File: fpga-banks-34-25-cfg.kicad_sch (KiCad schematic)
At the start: 49 parts, among them J13 PinHeader_1x3_P2.54mm_Drill1.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, Q12 2N7002_SOT-23-3, Q13 2N7002_SOT-23-3, Q14 2N7002_SOT-23-3, Q15 2N7002_SOT-23-3, Q16 2N7002_SOT-23-3, U14 XC7A100T-FGG484

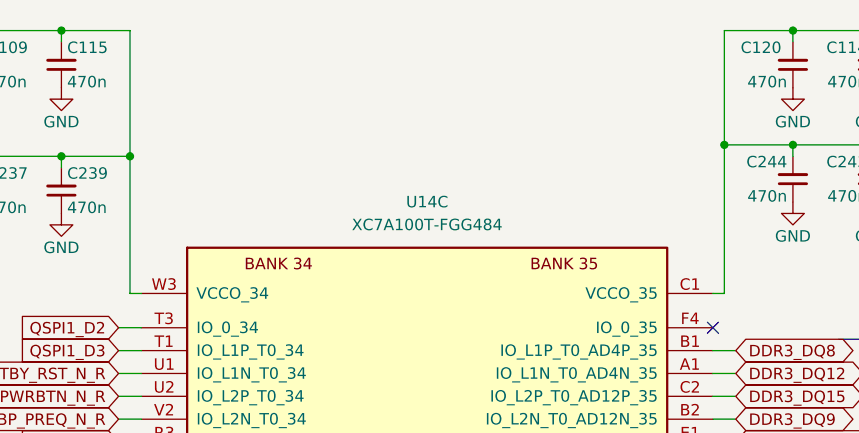
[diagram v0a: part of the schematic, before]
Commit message: ddr3 routing finished
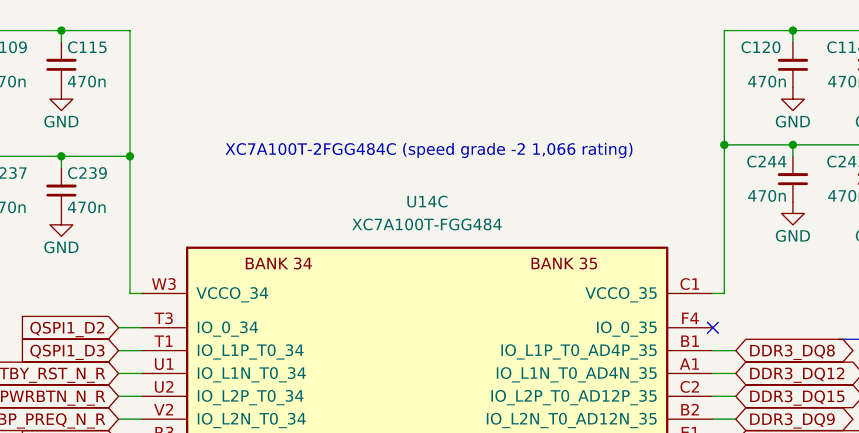
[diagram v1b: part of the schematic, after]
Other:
- note added: "XC7A100T-2FGG484C (speed grade -2 1,066 rating)"
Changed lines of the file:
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@@
+		)
+	)
+	(text "XC7A100T-2FGG484C (speed grade -2 1,066 rating)"
+		(exclude_from_sim no)
+		(at 299.974 57.912 0)
+		(effects
+			(font
+				(size 1.27 1.27)
+			)
 		)
 	)

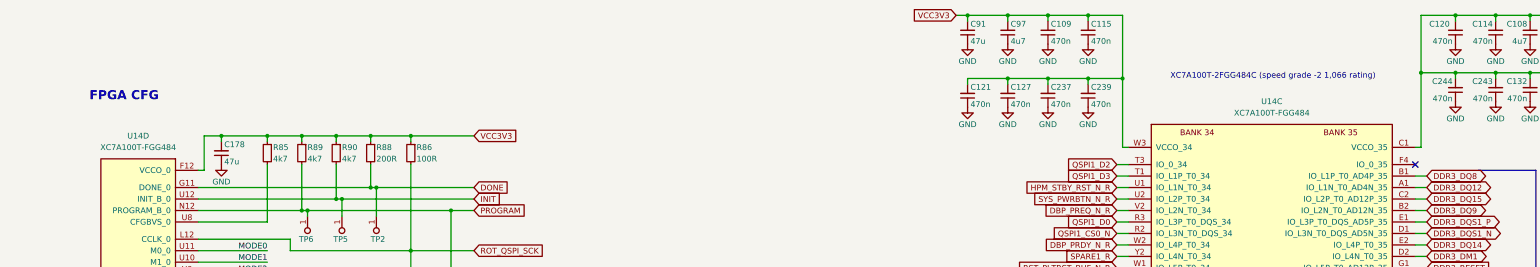
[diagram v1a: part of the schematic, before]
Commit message: a lot of routing and almost all caps of the fpga are placed down
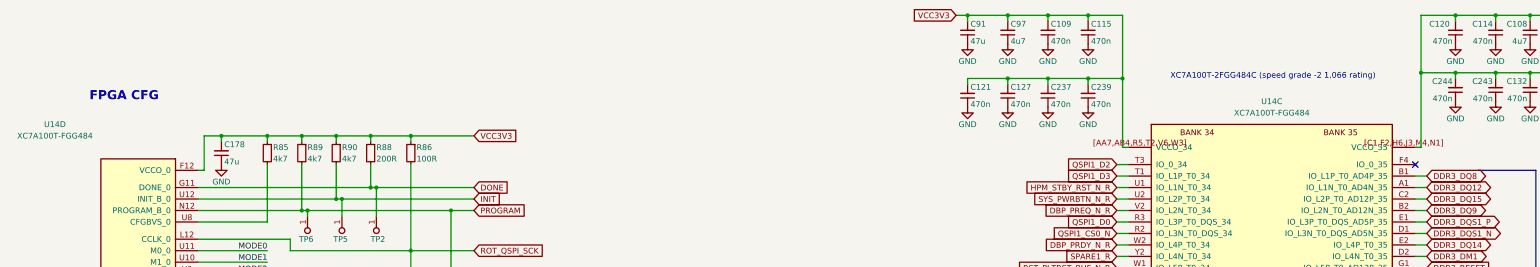
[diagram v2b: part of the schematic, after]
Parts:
- C102, C108, C97: footprint antmicro-footprints:C_0603_1608Metric -> Capacitor_SMD:C_0603_1608Metric; MPN C1608X5R1V475M080AC -> C0603C475K9PAC; Manufacturer TDK -> KEMET
- C109, C114, C115, C120, C121, C126, C127, C132, C237, C239, C243, C244: footprint antmicro-footprints:C_0402_1005Metric -> Capacitor_SMD:C_0402_1005Metric
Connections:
- net VCC1V35: now also U14.[C1,F2,H6,J3,M4,N1] (VCCO_35); no longer U14.C1 (VCCO_35), U14.F2 (VCCO_35), U14.H6 (VCCO_35), U14.J3 (VCCO_35), U14.M4 (VCCO_35), U14.N1 (VCCO_35)
- net VCC3V3: now also U14.[AA7,AB4,R5,T2,V6,W3] (VCCO_34); no longer U14.AA7 (VCCO_34), U14.AB4 (VCCO_34), U14.R5 (VCCO_34), U14.T2 (VCCO_34), U14.V6 (VCCO_34), U14.W3 (VCCO_34)
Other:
- moved on the sheet: U14C

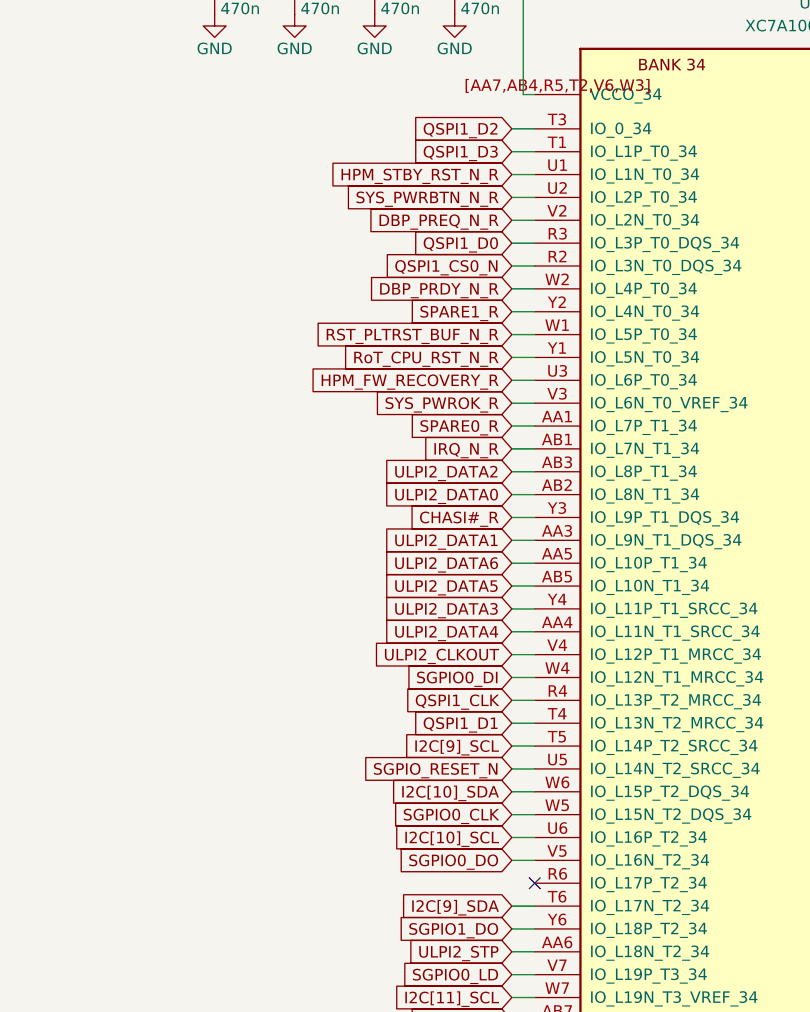
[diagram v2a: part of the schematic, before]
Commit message: a lot of poin swaps
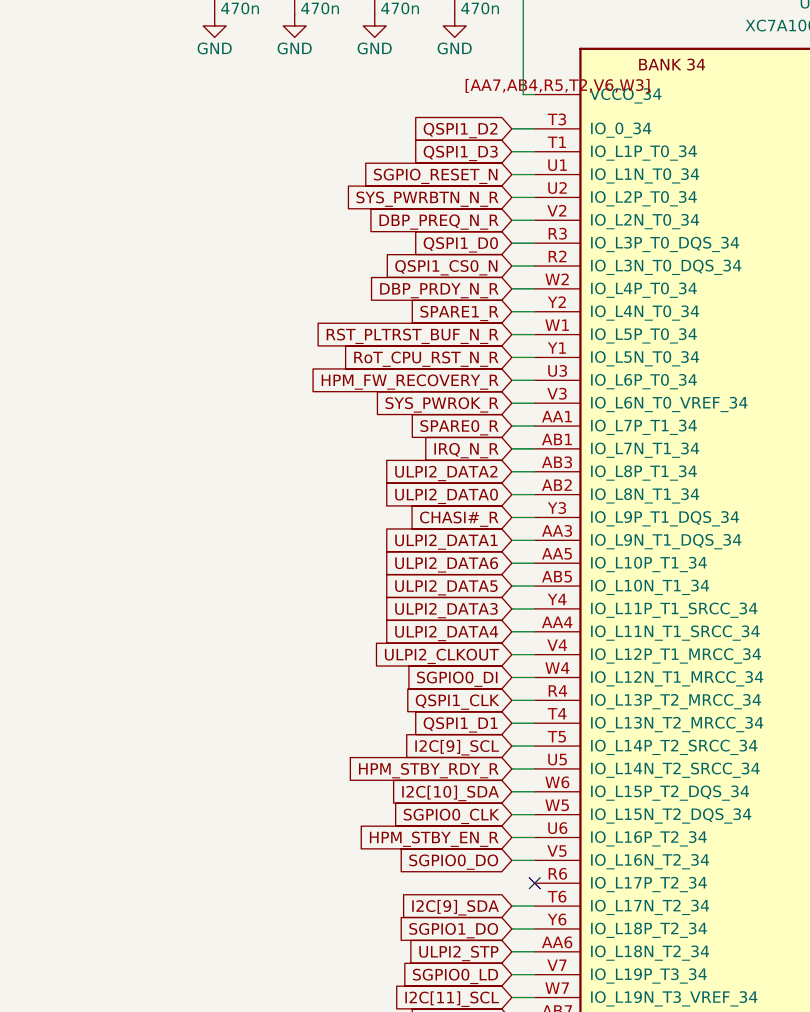
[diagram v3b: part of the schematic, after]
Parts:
- C109, C114, C115, C120, C121, C126, C127, C132, C237, C239, C243, C244: MPN C1005X5R1E474M050BB -> GXT155C80J474KE01D; Manufacturer TDK -> Murata Electronics
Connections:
- net HPM_STBY_RST_N_R is gone; now on net SGPIO_RESET_N: U14.U1 (IO_L1N_T0_34)
- net SGPIO_RESET_N: no longer U14.U5 (IO_L14N_T2_SRCC_34)
- net I2C[10]_SCL renamed HPM_STBY_EN_R
- new net HPM_STBY_RDY_R: U14.U5 (IO_L14N_T2_SRCC_34)

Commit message: river routing
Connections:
- net SGPIO0_DI is gone; now on net SYS_PWROK_R: U14.W4 (IO_L12N_T1_MRCC_34)
- net CHASI#_R: now also U14.Y7 (IO_L23N_T3_34); no longer U14.Y3 (IO_L9P_T1_DQS_34)
- net DBP_PRDY_N_R: now also U14.W5 (IO_L15N_T2_DQS_34); no longer U14.W2 (IO_L4P_T0_34)
- net DBP_PREQ_N_R: now also U14.Y3 (IO_L9P_T1_DQS_34); no longer U14.V2 (IO_L2N_T0_34)
- net I2C[10]_SDA: now also U14.W1 (IO_L5P_T0_34); no longer U14.W6 (IO_L15P_T2_DQS_34)
- net I2C[11]_SCL: now also U14.Y2 (IO_L4N_T0_34); no longer U14.W7 (IO_L19N_T3_VREF_34)
- net IRQ_N_R: now also U14.Y8 (IO_L23P_T3_34); no longer U14.AB1 (IO_L7N_T1_34)
- net RST_PLTRST_BUF_N_R: now also U14.W6 (IO_L15P_T2_DQS_34); no longer U14.W1 (IO_L5P_T0_34)
- net RSVD2: now also U14.V2 (IO_L2N_T0_34); no longer U14.Y7 (IO_L23N_T3_34)
- net RoT_CPU_RST_N_R: now also U14.V7 (IO_L19P_T3_34); no longer U14.Y1 (IO_L5N_T0_34)
- net SGPIO0_CLK: now also U14.W2 (IO_L4P_T0_34); no longer U14.W5 (IO_L15N_T2_DQS_34)
- net SGPIO0_DO: now also U14.U2 (IO_L2P_T0_34); no longer U14.V5 (IO_L16N_T2_34)
- net SGPIO0_LD: now also U14.Y1 (IO_L5N_T0_34); no longer U14.V7 (IO_L19P_T3_34)
- net SGPIO1_DI: now also U14.AB1 (IO_L7N_T1_34); no longer U14.Y8 (IO_L23P_T3_34)
- net SGPIO1_DO: now also U14.AA1 (IO_L7P_T1_34); no longer U14.Y6 (IO_L18P_T2_34)
- net SPARE0_R: now also U14.W7 (IO_L19N_T3_VREF_34); no longer U14.AA1 (IO_L7P_T1_34)
- net SPARE1_R: now also U14.Y6 (IO_L18P_T2_34); no longer U14.Y2 (IO_L4N_T0_34)
- net SYS_PWRBTN_N_R: now also U14.V5 (IO_L16N_T2_34); no longer U14.U2 (IO_L2P_T0_34)
- net SYS_PWROK_R: no longer U14.V3 (IO_L6N_T0_VREF_34)
- new net HPM_STBY_RST_N_R: U14.V3 (IO_L6N_T0_VREF_34)

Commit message: Almost done with the routing
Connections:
- net I2C[9]_SCL is gone; now on net I2C[11]_SDA: U14.T5 (IO_L14P_T2_SRCC_34)
- net I2C[9]_SDA is gone; now on net I2C[11]_SCL: U14.T6 (IO_L17N_T2_34)
- net SGPIO_INTR_N is gone; now on net I2C[10]_SDA: U14.U7 (IO_25_34)
- net I2C[10]_SDA: no longer U14.W1 (IO_L5P_T0_34)
- net I2C[11]_SCL: no longer U14.Y2 (IO_L4N_T0_34)
- net I2C[11]_SDA: no longer U14.W9 (IO_L24P_T3_34)
- net I2C[12]_SDA: now also U14.U1 (IO_L1N_T0_34); no longer U14.V9 (IO_L21P_T3_DQS_34)
- net RSVD2: now also U14.V9 (IO_L21P_T3_DQS_34); no longer U14.V2 (IO_L2N_T0_34)
- net SGPIO0_CLK: now also U14.Y9 (IO_L24N_T3_34); no longer U14.W2 (IO_L4P_T0_34)
- net SGPIO0_DO: now also U14.W1 (IO_L5P_T0_34); no longer U14.U2 (IO_L2P_T0_34)
- net SGPIO1_DI: now also U14.AA1 (IO_L7P_T1_34); no longer U14.AB1 (IO_L7N_T1_34)
- net SGPIO1_DO: now also U14.AB1 (IO_L7N_T1_34); no longer U14.AA1 (IO_L7P_T1_34)
- net SGPIO1_LD: now also U14.Y2 (IO_L4N_T0_34); no longer U14.Y9 (IO_L24N_T3_34)
- net SGPIO_RESET_N: now also U14.W9 (IO_L24P_T3_34); no longer U14.U1 (IO_L1N_T0_34)
- net I2C[12]_SCL renamed I2C[10]_SCL
- new net I2C[5]_SCL: U14.U2 (IO_L2P_T0_34)
- new net I2C[5]_SDA: U14.V2 (IO_L2N_T0_34)
- new net SGPIO0_DI: U14.W2 (IO_L4P_T0_34)

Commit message: bom changes
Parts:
- R81, R82, R83, R84: MPN ERJ2GE0R00X -> RC0402JR-7D0RL; Manufacturer Panasonic -> YAGEO

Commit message: version 1.0 complete
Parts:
- C178, C91, C96: MPN C1210C476K8RACTU -> C1210C476K8RAC7210
- D10, D11, D12, D13, D9: MPN LG L29K-G2J1-24-Z -> SML-D13FWT86C; Manufacturer OSRAM -> ROHM Semiconductor
- R85, R89, R90: MPN CR0402-FX-4701GLF -> RC0402FR-7D4K7L; Manufacturer Bourns -> YAGEO
- R86, R87: MPN CR0402-FX-1000GLF -> RC0402FR-7D100RL; Manufacturer Bourns -> YAGEO
- U14: MPN XC7A100T-FGG484 -> XC7A100T-2FGG484C

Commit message: "In the process of upgrading the ddr memory"
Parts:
- C178, C91, C96: footprint antmicro-footprints:C_1210_3225Metric -> Capacitor_SMD:C_1210_3225Metric
- R128, R129, R130, R131, R132, R81, R82, R83, R84, R85, R86, R87, R88, R89, R90: footprint antmicro-footprints:R_0402_1005Metric -> Resistor_SMD:R_0402_1005Metric
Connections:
- net VCC1V35: now also C109.2, C115.2, C121.2, C127.2, C237.2, C239.2, C91.2, C97.2, U14.[AA7,AB4,R5,T2,V6,W3] (VCCO_34)
- net VCC3V3: no longer C109.2, C115.2, C121.2, C127.2, C237.2, C239.2, C91.2, C97.2, U14.[AA7,AB4,R5,T2,V6,W3] (VCCO_34)
- net A12: now reaches U14.R6 (IO_L17P_T2_34)
- net CHASI#_R renamed DQL17
- net DBP_PRDY_N_R renamed A9
- net DBP_PREQ_N_R renamed DQS.DQSU
- net DDR3_A0 renamed Control.ODT1
- net DDR3_A1 renamed A6
- net DDR3_A10 renamed Control.CAS#
- net DDR3_A11 renamed A2
- net DDR3_A12: no longer names the net of U14.L6 (IO_25_35)
- net DDR3_A13 renamed A1
- net DDR3_A14 renamed BA2
- net DDR3_A2 renamed Control.ODT0
- net DDR3_A3 renamed Control.CS1#
- net DDR3_A4 renamed A4
- net DDR3_A5 renamed A7
- net DDR3_A6 renamed A0
- net DDR3_A7 renamed A8
- net DDR3_A8 renamed A3
- net DDR3_A9 renamed A5
- net DDR3_BA0 renamed Control.CKE1
- net DDR3_BA1 renamed Control.CS0#
- net DDR3_BA2 renamed BA1
- net DDR3_CAS renamed Control.RAS#
- net DDR3_CKE renamed BA0
- net DDR3_CLK_N renamed Clk.CK#
- net DDR3_CLK_P renamed Clk.CK
- net DDR3_DM0 renamed DQL07
- net DDR3_DM1 renamed DQU05
- net DDR3_DQ0 renamed DQL02
- net DDR3_DQ1 renamed DQL06
- net DDR3_DQ10 renamed DQU06
- net DDR3_DQ11 renamed DQU07
- net DDR3_DQ12 renamed DQU01
- net DDR3_DQ13 renamed DMU00
- net DDR3_DQ14 renamed DQU04
- net DDR3_DQ15 renamed DQU02
- net DDR3_DQ2 renamed DQL04
- net DDR3_DQ3 renamed DQL03
- net DDR3_DQ4 renamed DML00
- net DDR3_DQ5 renamed DQL01
- net DDR3_DQ6 renamed DQL05
- net DDR3_DQ7 renamed DQL00
- net DDR3_DQ8 renamed DQU00
- net DDR3_DQ9 renamed DQU03
- net DDR3_DQS0_N renamed DQS_1.DQSL#
- net DDR3_DQS0_P renamed DQS_1.DQSL
- net DDR3_DQS1_N renamed DQS_1.DQSU#
- net DDR3_DQS1_P renamed DQS_1.DQSU
- net DDR3_ODT renamed Control.CKE0
- net DDR3_RAS renamed Control.Reset#
- net DDR3_WE renamed Control.WE#
- net HPM_FW_RECOVERY_R: no longer names the net of U14.U3 (IO_L6P_T0_34)
- net HPM_STBY_EN_R renamed A10
- net HPM_STBY_RDY_R: no longer names the net of U14.U5 (IO_L14N_T2_SRCC_34)
- net HPM_STBY_RST_N_R: no longer names the net of U14.V3 (IO_L6N_T0_VREF_34)
- net I2C[10]_SCL renamed DQS.DQSL#
- net I2C[10]_SDA: no longer names the net of U14.U7 (IO_25_34)
- net I2C[11]_SCL renamed A13
- net I2C[11]_SDA: no longer names the net of U14.T5 (IO_L14P_T2_SRCC_34)
- net I2C[12]_SDA: no longer names the net of U14.U1 (IO_L1N_T0_34)
- net I2C[5]_SCL: no longer names the net of U14.U2 (IO_L2P_T0_34)
- net I2C[5]_SDA: no longer names the net of U14.V2 (IO_L2N_T0_34)
- net IRQ_N_R renamed DQL16
- net QSPI1_CLK: no longer names the net of U14.R4 (IO_L13P_T2_MRCC_34)
- net QSPI1_CS0_N: no longer names the net of U14.R2 (IO_L3N_T0_DQS_34)
- net QSPI1_D0: no longer names the net of U14.R3 (IO_L3P_T0_DQS_34)
- net QSPI1_D1: no longer names the net of U14.T4 (IO_L13N_T2_MRCC_34)
- net QSPI1_D2: no longer names the net of U14.T3 (IO_0_34)
- net QSPI1_D3: no longer names the net of U14.T1 (IO_L1P_T0_34)
- net ROT_QSPI_SCK renamed QSPI_SCK
- net RST_PLTRST_BUF_N_R: no longer names the net of U14.W6 (IO_L15P_T2_DQS_34)
- net RSVD2 renamed DQS.DQSL
- net RoT_CPU_RST_N_R renamed DQL10
- net SGPIO0_CLK: no longer names the net of U14.Y9 (IO_L24N_T3_34)
- net SGPIO0_DI: no longer names the net of U14.W2 (IO_L4P_T0_34)
- net SGPIO0_DO: no longer names the net of U14.W1 (IO_L5P_T0_34)
- net SGPIO0_LD: no longer names the net of U14.Y1 (IO_L5N_T0_34)
- net SGPIO1_DI: no longer names the net of U14.AA1 (IO_L7P_T1_34)
- net SGPIO1_DO renamed DQU10
- net SGPIO1_LD: no longer names the net of U14.Y2 (IO_L4N_T0_34)
- net SGPIO_RESET_N renamed DML1
- net SPARE0_R renamed DQL11
- net SPARE1_R renamed A14
- net SYS_PWRBTN_N_R renamed A11
- net SYS_PWROK_R renamed DMU1
- net ULPI2_CLKOUT renamed DQU17
- net ULPI2_DATA0 renamed DQU12
- net ULPI2_DATA1 renamed DQS.DQSU#
- net ULPI2_DATA2 renamed DQU11
- net ULPI2_DATA3 renamed DQU15
- net ULPI2_DATA4 renamed DQU16
- net ULPI2_DATA5 renamed DQU14
- net ULPI2_DATA6 renamed DQU13
- net ULPI2_DATA7 renamed DQL13
- net ULPI2_DIR renamed DQL12
- net ULPI2_NXT renamed DQL15
- net ULPI2_RESET renamed DQL14
- net ULPI2_STP renamed A15
- no-connect marks 3 -> 24
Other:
- added sheet DDR3L_0 (DDR3L_0.kicad_sch)
- added sheet DDR3L_1 (DDR3L_1.kicad_sch)
- note added: "ADD/CTRL"
- note added: "DATA"
- note added: "Termination!!"
- note removed: "DDR3"
